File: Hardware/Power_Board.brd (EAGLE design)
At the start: 160 x 100 mm, 41 parts, among them K1 E3206S, K2 E3206S, K3 E3206S, K4 E3206S, K5 E3206S, K6 E3206S, Q1 BD135, Q2 BD135, Q3 BD135, Q4 BD135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

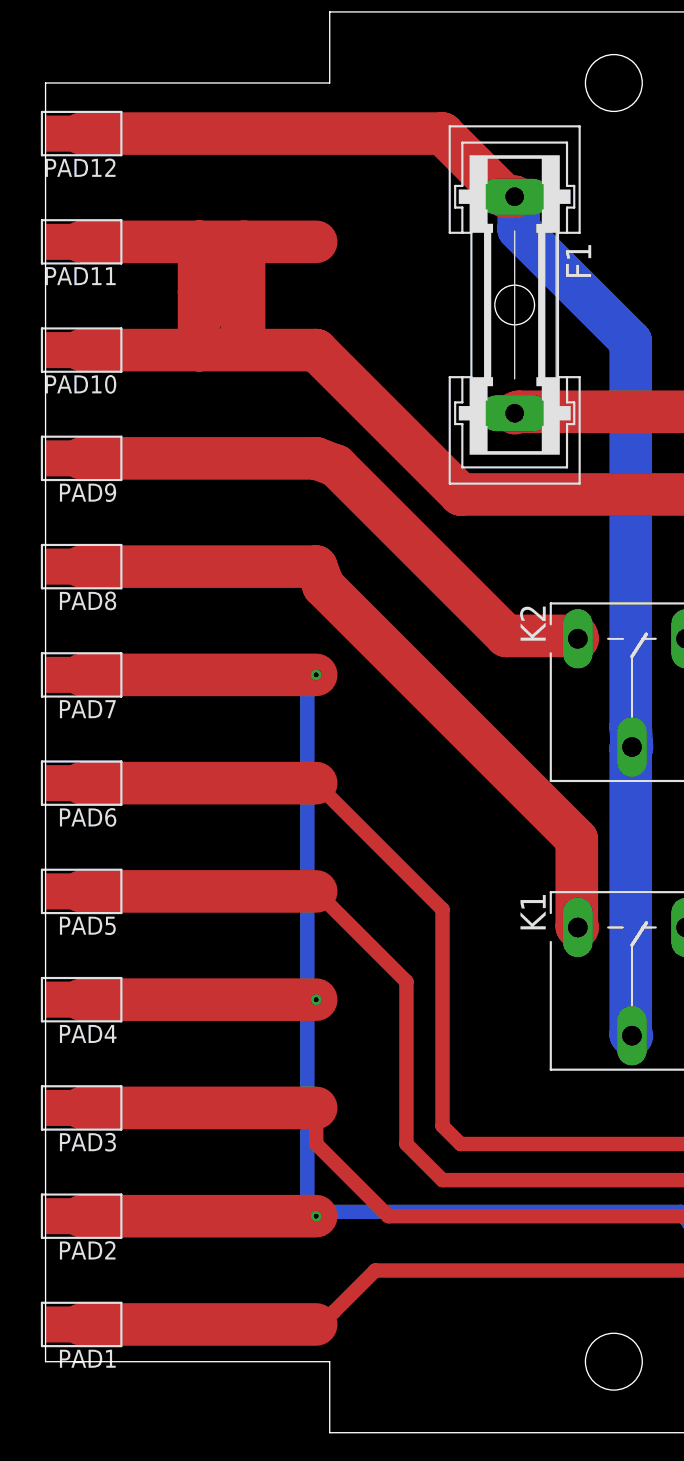
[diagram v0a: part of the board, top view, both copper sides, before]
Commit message: Added bigger pads to the power board PCB, so the PCB coating won't recover the pads.
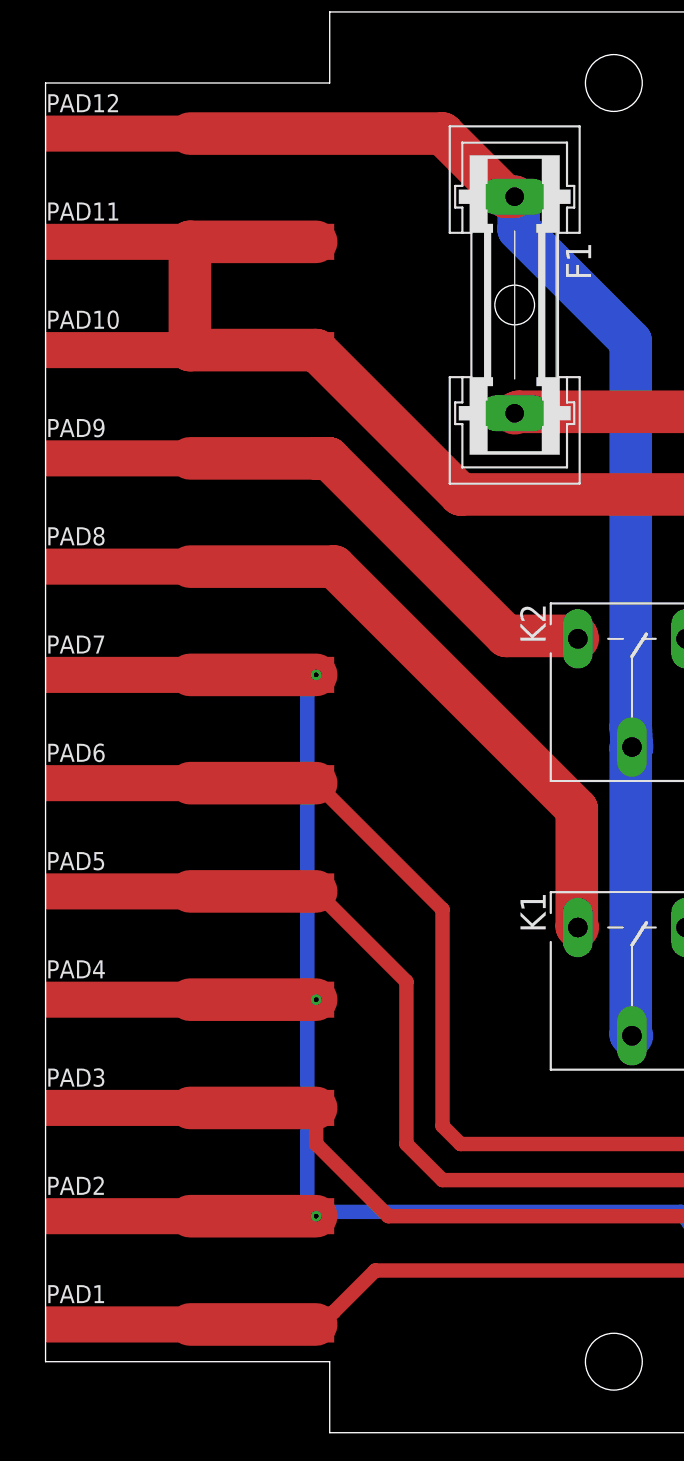
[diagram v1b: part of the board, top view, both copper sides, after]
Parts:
- PAD1: value WIREPADSMD5-2,5 -> Internal thermistor; device wirepad:5-2,5 -> Pad:SMD2,54-20,32
- PAD10, PAD11: value WIREPADSMD5-2,5 -> Neutral; device wirepad:5-2,5 -> Pad:SMD2,54-20,32
- PAD12: value WIREPADSMD5-2,5 -> Live; device wirepad:5-2,5 -> Pad:SMD2,54-20,32
- PAD2, PAD4, PAD7: value WIREPADSMD5-2,5 -> GND; device wirepad:5-2,5 -> Pad:SMD2,54-20,32
- PAD3: value WIREPADSMD5-2,5 -> Night trimmer; device wirepad:5-2,5 -> Pad:SMD2,54-20,32
- PAD5: value WIREPADSMD5-2,5 -> Day trimmer; device wirepad:5-2,5 -> Pad:SMD2,54-20,32
- PAD6: value WIREPADSMD5-2,5 -> External thermistor; device wirepad:5-2,5 -> Pad:SMD2,54-20,32
- PAD8: value WIREPADSMD5-2,5 -> Mixing valve colder; device wirepad:5-2,5 -> Pad:SMD2,54-20,32
- PAD9: value WIREPADSMD5-2,5 -> Mixing valve hotter; device wirepad:5-2,5 -> Pad:SMD2,54-20,32
- turned PAD1 to 270 degrees
- turned PAD10 to 270 degrees
- turned PAD11 to 270 degrees
- turned PAD12 to 270 degrees
- turned PAD2 to 270 degrees
- turned PAD3 to 270 degrees
- turned PAD4 to 270 degrees
- turned PAD5 to 270 degrees
- turned PAD6 to 270 degrees
- turned PAD7 to 270 degrees
- turned PAD8 to 270 degrees
- turned PAD9 to 270 degrees
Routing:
- net N$27: track 120.3 -> 91.0 mm
- net GND: track 329.7 -> 306.8 mm
- net PIN4: track 64.7 -> 57.1 mm
- net N$8: track 87.1 -> 79.4 mm
- net N$10: track 94.9 -> 87.2 mm
- net N$1: track 79.2 -> 71.5 mm
- net N$2: track 54.8 -> 47.2 mm
- net N$3: track 49.4 -> 42.7 mm
- net N$6: track 40.1 -> 33.5 mm
